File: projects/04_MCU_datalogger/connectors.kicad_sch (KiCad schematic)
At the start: 4 parts, among them J1 Conn_01x04_Pin, J2 Conn_01x09_Pin, J3 Conn_01x04_Pin, J4 Conn_02x03_Odd_Even

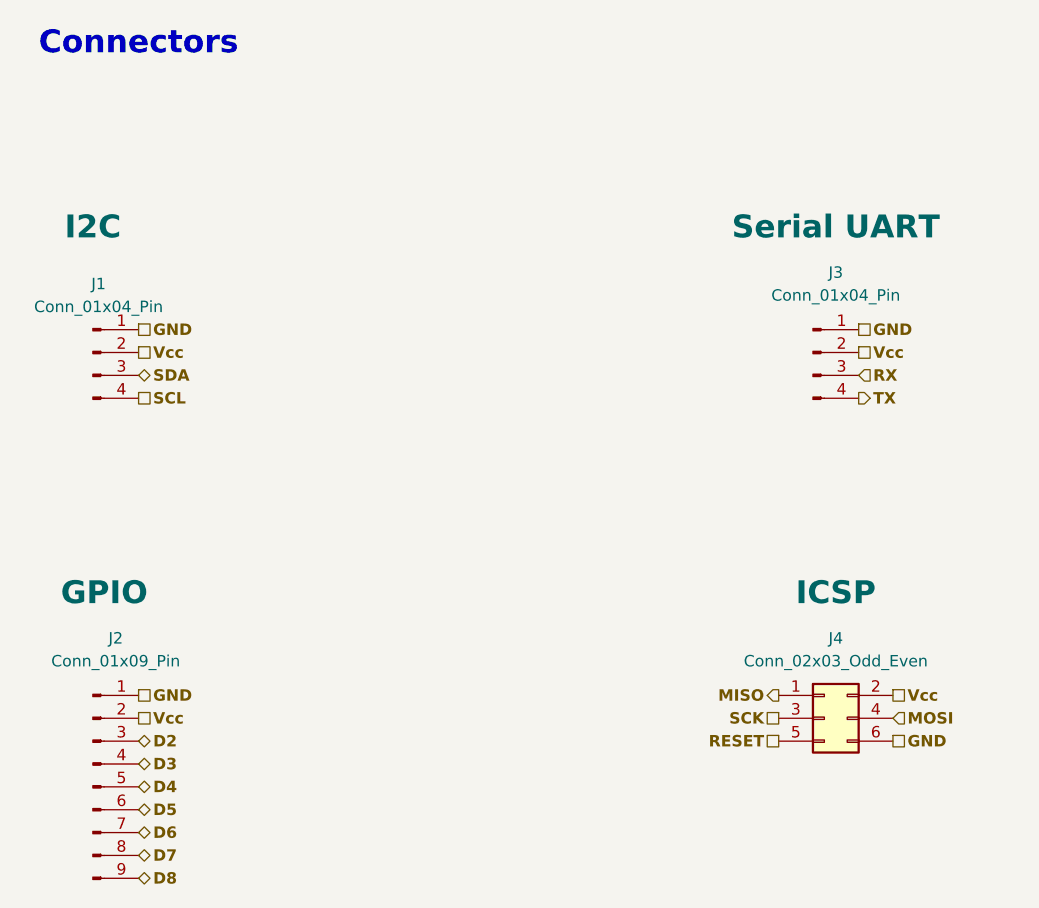
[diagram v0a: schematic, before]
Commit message: MCU datalogger - clean up schematic
In `MCU_datalogger.kicad_sch` and `connectors.kicad_sch`:
- update RTC, EEPROM, Crystal symbols to arrange pins properly
  and align to 100 mil grid
- clean up schematic
- rename nets to start with ICSP_* I2C_* UART_*
- replace Vcc label with VCC power symbol
- add net colors

In `MCU_datalogger.kicad_pcb`:
- replace layout in main branch with empty placeholder referring to 2layer and 4layer branches

Notes:
- ensure modified symbols are saved in custom library (e.g. MH_library)
- before deleting the layout DRC threw hundreds of errors: unconnected pins, solder mask bridges, etc. (WHY?)
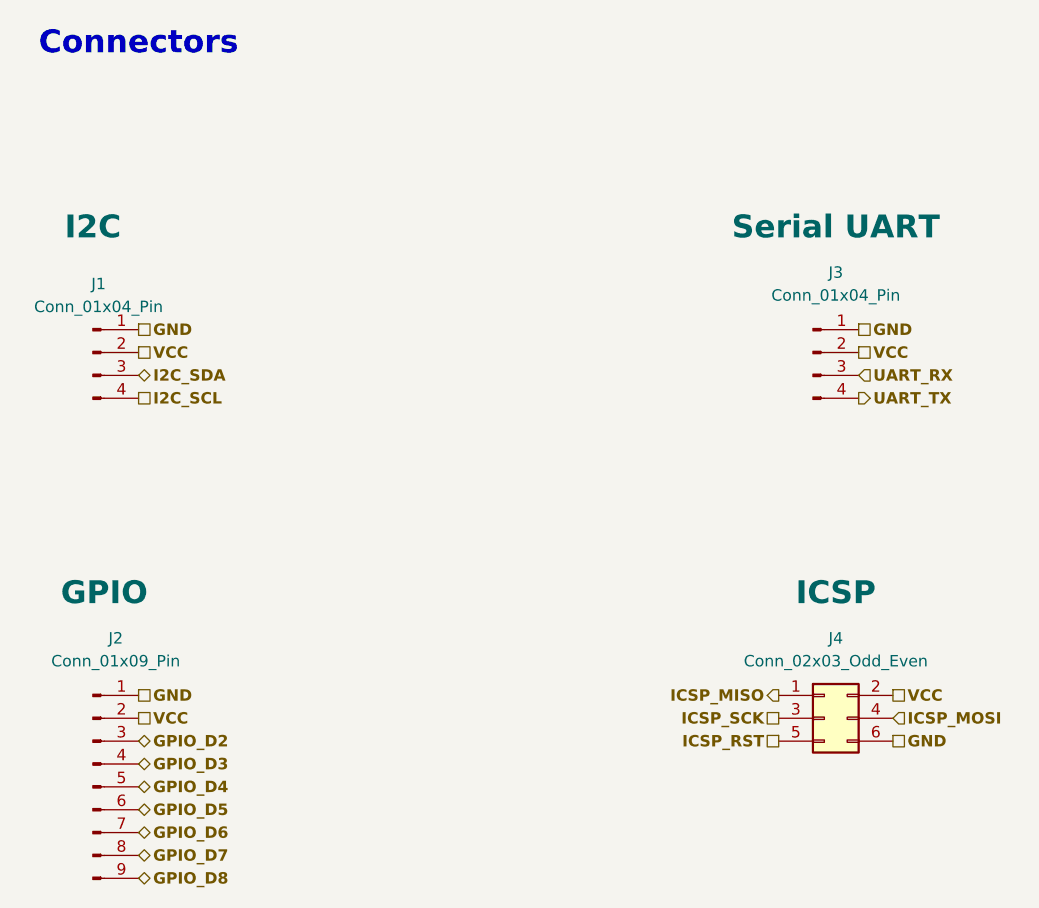
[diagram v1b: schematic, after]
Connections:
- net D2 renamed GPIO_D2
- net D3 renamed GPIO_D3
- net D4 renamed GPIO_D4
- net D5 renamed GPIO_D5
- net D6 renamed GPIO_D6
- net D7 renamed GPIO_D7
- net D8 renamed GPIO_D8
- net MISO renamed ICSP_MISO
- net MOSI renamed ICSP_MOSI
- net RESET renamed ICSP_RST
- net RX renamed UART_RX
- net SCK renamed ICSP_SCK
- net SCL renamed I2C_SCL
- net SDA renamed I2C_SDA
- net TX renamed UART_TX
- net Vcc renamed VCC
